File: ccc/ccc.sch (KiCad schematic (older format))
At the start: 36 parts, among them J1 Conn_02x03_Odd_Even, U1 rt9013-33, U2 LTC3225-1

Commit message: usb bridge readability update
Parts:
- added R? (x2): 10k, symbol Device:R
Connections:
- net GPIO0: now also Q?.2 (C); no longer Q?.2 (C)
- net RST: now also Q?.2 (C); no longer Q?.2 (C)
- new net: Q?.3 (E), R?.2, U?.24 (~RTS)
- new net: Q?.3 (E), R?.2, U?.28 (~DTR)
- new net: Q?.1 (B), R?.1 (x2)
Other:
- moved on the sheet: Q?, R?
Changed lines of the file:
@@
 L Device:Q_NPN_BCE Q?
 U 1 1 5D00C58E
-P 4600 4700
-F 0 "Q?" H 4791 4654 50  0000 L CNN
-F 1 "Q_NPN_BCE" H 4791 4745 50  0000 L CNN
-F 2 "" H 4800 4800 50  0001 C CNN
-F 3 "~" H 4600 4700 50  0001 C CNN
-	1    4600 4700
-	0    1    -1   0
+P 4600 5050
+F 0 "Q?" H 4791 5004 50  0000 L CNN
+F 1 "Q_NPN_BCE" H 4791 5095 50  0000 L CNN
+F 2 "" H 4800 5150 50  0001 C CNN
+F 3 "~" H 4600 5050 50  0001 C CNN
+	1    4600 5050
+	1    0    0    1
 $EndComp
 $Comp
 L Device:Q_NPN_BCE Q?
 U 1 1 5D00EDC1
-P 4600 5200
-F 0 "Q?" H 4791 5246 50  0000 L CNN
-F 1 "Q_NPN_BCE" H 4791 5155 50  0000 L CNN
-F 2 "" H 4800 5300 50  0001 C CNN
-F 3 "~" H 4600 5200 50  0001 C CNN
-	1    4600 5200
-	0    -1   1    0
-$EndComp
-Wire Wire Line
-	3350 5050 2900 5050
-Wire Wire Line
-	4400 4600 4400 5000
-Wire Wire Line
-	4400 5000 4600 5000
-Connection ~ 4400 4600
+P 4600 4400
+F 0 "Q?" H 4791 4446 50  0000 L CNN
+F 1 "Q_NPN_BCE" H 4791 4355 50  0000 L CNN
+F 2 "" H 4800 4500 50  0001 C CNN
+F 3 "~" H 4600 4400 50  0001 C CNN
+	1    4600 4400
+	1    0    0    -1
+$EndComp
 Wire Wire Line
 	2900 5450 3500 5450
-Text GLabel 5100 4600 2    50   Input ~ 0
+Text GLabel 5150 4050 2    50   Input ~ 0
 RST
-Wire Wire Line
-	4800 4600 5100 4600
-Wire Wire Line
-	4600 4900 4800 4900
-Wire Wire Line
-	4800 4900 4800 5300
-Connection ~ 4600 4900
-Text GLabel 4050 5800 3    50   Input ~ 0
+Text GLabel 5800 5250 2    50   Input ~ 0
 GPIO0
 Wire Wire Line
@@
 L Device:R R?
 U 1 1 5D0A7656
-P 4050 5400
-F 0 "R?" H 4120 5446 50  0000 L CNN
-F 1 "10k" H 4120 5355 50  0000 L CNN
-F 2 "" V 3980 5400 50  0001 C CNN
-F 3 "~" H 4050 5400 50  0001 C CNN
-	1    4050 5400
+P 5550 4800
+F 0 "R?" H 5620 4846 50  0000 L CNN
+F 1 "10k" H 5620 4755 50  0000 L CNN
+F 2 "" V 5480 4800 50  0001 C CNN
+F 3 "~" H 5550 4800 50  0001 C CNN
+	1    5550 4800
 	1    0    0    -1
 $EndComp
@@
 L power:+3V3 #PWR?
 U 1 1 5D0A810F
-P 4050 5250
-F 0 "#PWR?" H 4050 5100 50  0001 C CNN
-F 1 "+3V3" H 4065 5423 50  0000 C CNN
-F 2 "" H 4050 5250 50  0001 C CNN
-F 3 "" H 4050 5250 50  0001 C CNN
-	1    4050 5250
-	1    0    0    -1
-$EndComp
-Wire Wire Line
-	4350 5550 4350 5300
-Wire Wire Line
-	4350 5300 4400 5300
-Wire Wire Line
-	4050 5550 4350 5550
-Wire Wire Line
-	4050 5550 4050 5800
-Connection ~ 4050 5550
-Wire Wire Line
-	3350 5050 3350 4600
-Wire Wire Line
-	3350 4600 4400 4600
-Wire Wire Line
-	3500 5450 3500 4900
-Wire Wire Line
-	3500 4900 4600 4900
+P 5550 4650
+F 0 "#PWR?" H 5550 4500 50  0001 C CNN
+F 1 "+3V3" H 5565 4823 50  0000 C CNN
+F 2 "" H 5550 4650 50  0001 C CNN
+F 3 "" H 5550 4650 50  0001 C CNN
+	1    5550 4650
+	1    0    0    -1
+$EndComp
 Text GLabel 10850 3500 2    50   Input ~ 0
 GPIO0
@@
 Wire Wire Line
 	10700 3550 10600 3550
-Text GLabel 6350 5850 2    50   Input ~ 0
+Text GLabel 6300 4050 2    50   Input ~ 0
 GPIO2
 $Comp
 L Device:R R?
 U 1 1 5D15E953
-P 6200 5550
-F 0 "R?" H 6270 5596 50  0000 L CNN
-F 1 "10k" H 6270 5505 50  0000 L CNN
-F 2 "" V 6130 5550 50  0001 C CNN
-F 3 "~" H 6200 5550 50  0001 C CNN
-	1    6200 5550
+P 6150 3750
+F 0 "R?" H 6220 3796 50  0000 L CNN
+F 1 "10k" H 6220 3705 50  0000 L CNN
+F 2 "" V 6080 3750 50  0001 C CNN
+F 3 "~" H 6150 3750 50  0001 C CNN
+	1    6150 3750
 	1    0    0    -1
 $EndComp
@@
 L power:+3V3 #PWR?
 U 1 1 5D15EFF7
-P 6200 5150
-F 0 "#PWR?" H 6200 5000 50  0001 C CNN
-F 1 "+3V3" H 6215 5323 50  0000 C CNN
-F 2 "" H 6200 5150 50  0001 C CNN
-F 3 "" H 6200 5150 50  0001 C CNN
-	1    6200 5150
-	1    0    0    -1
-$EndComp
-Wire Wire Line
-	6200 5150 6200 5400
-Wire Wire Line
-	6200 5850 6350 5850
-Wire Wire Line
-	6200 5700 6200 5850
+P 6150 3350
+F 0 "#PWR?" H 6150 3200 50  0001 C CNN
+F 1 "+3V3" H 6165 3523 50  0000 C CNN
+F 2 "" H 6150 3350 50  0001 C CNN
+F 3 "" H 6150 3350 50  0001 C CNN
+	1    6150 3350
+	1    0    0    -1
+$EndComp
+Wire Wire Line
+	6150 3350 6150 3600
+Wire Wire Line
+	6150 4050 6300 4050
+Wire Wire Line
+	6150 3900 6150 4050
 Text GLabel 8900 4950 2    50   Input ~ 0
 GPIO2
@@
 Wire Wire Line
 	10700 3950 10850 3950
+$Comp
+L Device:R R?
+U 1 1 5CECFF12
+P 4050 5050
+F 0 "R?" V 3843 5050 50  0000 C CNN
+F 1 "10k" V 3934 5050 50  0000 C CNN
+F 2 "" V 3980 5050 50  0001 C CNN
+F 3 "~" H 4050 5050 50  0001 C CNN
+	1    4050 5050
+	0    1    1    0
+$EndComp
+$Comp
+L Device:R R?
+U 1 1 5CED075B
+P 4050 4400
+F 0 "R?" V 3843 4400 50  0000 C CNN
+F 1 "10k" V 3934 4400 50  0000 C CNN
+F 2 "" V 3980 4400 50  0001 C CNN
+F 3 "~" H 4050 4400 50  0001 C CNN
+	1    4050 4400
+	0    1    1    0
+$EndComp
+Wire Wire Line
+	4200 4400 4400 4400
+Wire Wire Line
+	4200 5050 4400 5050
+Wire Wire Line
+	2900 5050 3750 5050
+Wire Wire Line
+	3500 4400 3850 4400
+Wire Wire Line
+	3500 4400 3500 5450
+Wire Wire Line
+	5150 4050 4700 4050
+Wire Wire Line
+	4700 4050 4700 4200
+Wire Wire Line
+	3750 5050 3750 4600
+Wire Wire Line
+	3750 4600 4700 4600
+Connection ~ 3750 5050
+Wire Wire Line
+	3750 5050 3900 5050
+Wire Wire Line
+	4700 4850 4700 4700
+Wire Wire Line
+	4700 4700 3850 4700
+Wire Wire Line
+	3850 4700 3850 4400
+Connection ~ 3850 4400
+Wire Wire Line
+	3850 4400 3900 4400
+Wire Wire Line
+	4700 5250 5550 5250
+Wire Wire Line
+	5800 5250 5550 5250
+Connection ~ 5550 5250
+Wire Wire Line
+	5550 4950 5550 5250
 $EndSCHEMATC

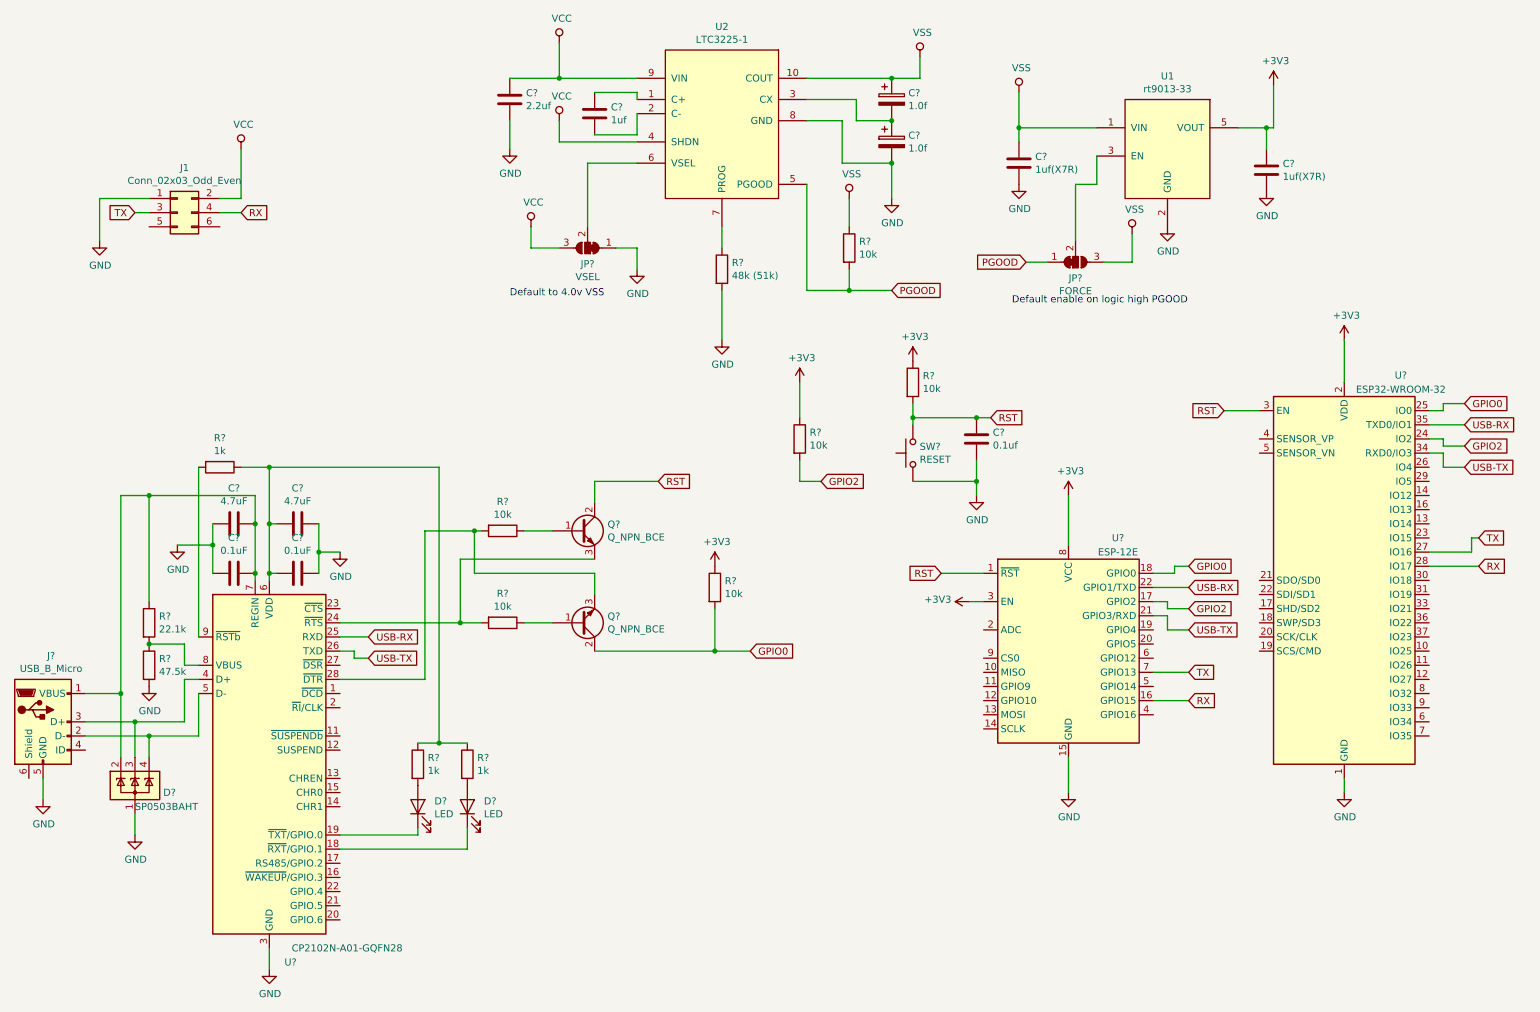
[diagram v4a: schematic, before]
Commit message: Removed usb bridge - added programming header
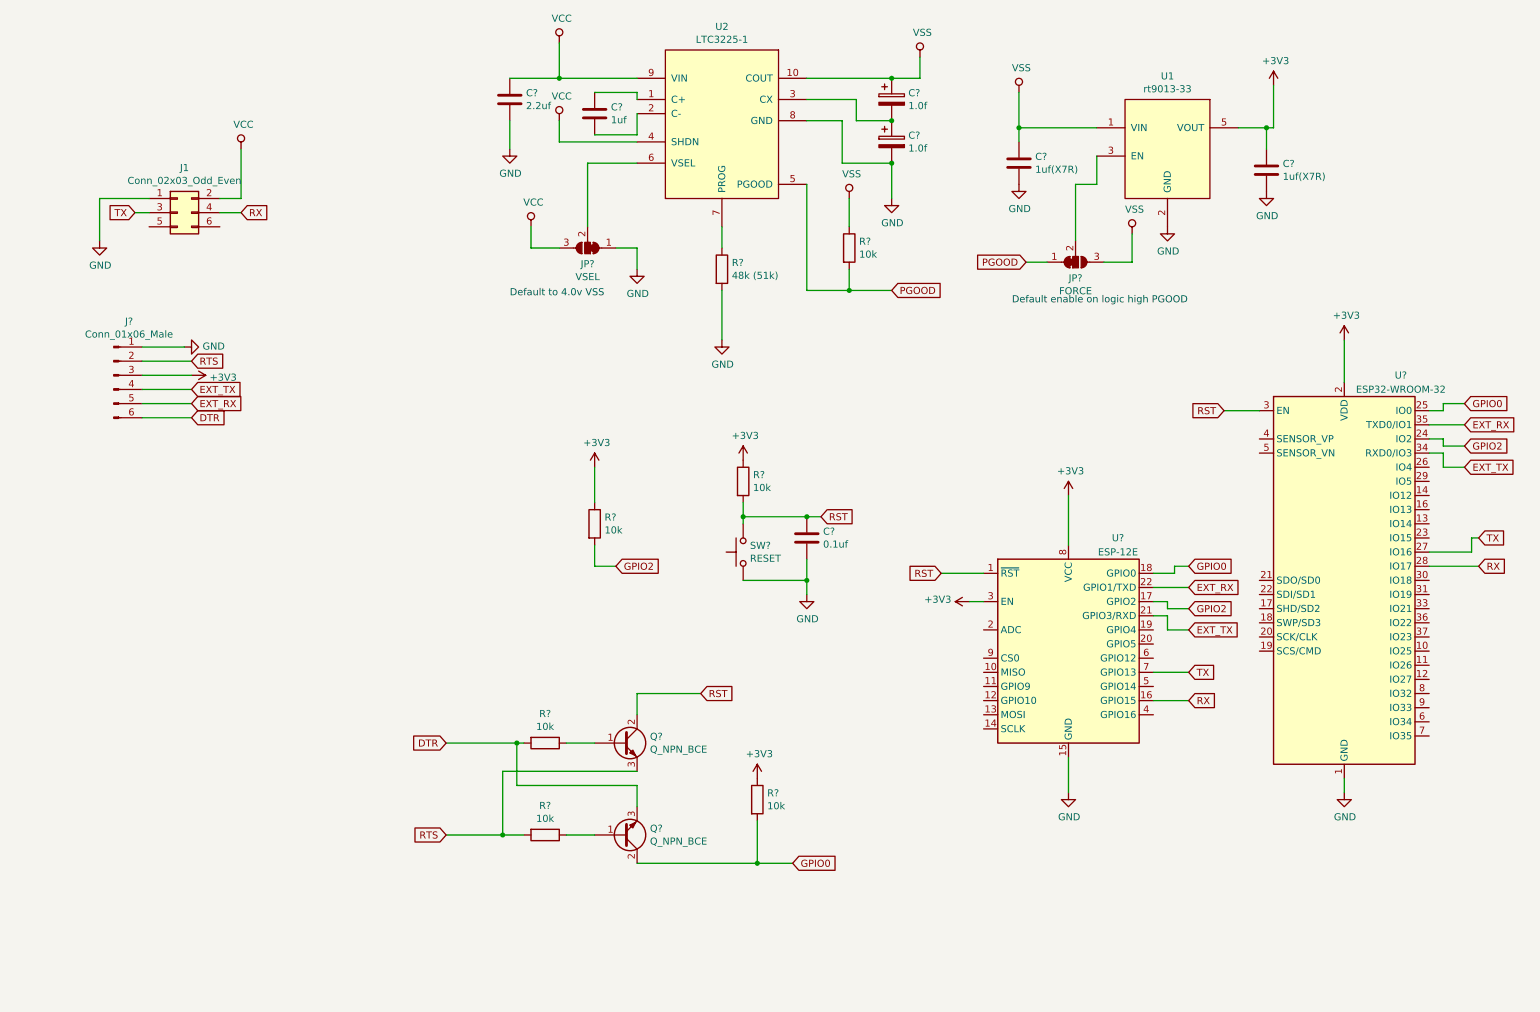
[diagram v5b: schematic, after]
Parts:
- removed C? (x2): 0.1uF, symbol Device:C
- removed C? (x2): 4.7uF, symbol Device:C
- removed D?: SP0503BAHT, Package_TO_SOT_SMD:SOT-143, symbol Power_Protection:SP0503BAHT
- removed D? (x2): LED, symbol Device:LED
- removed J?: USB_B_Micro, symbol Connector:USB_B_Micro
- removed R?: 22.1k, symbol Device:R
- removed R?: 47.5k, symbol Device:R
- removed R? (x3): 1k, symbol Device:R
- removed U?: CP2102N-A01-GQFN28, Package_DFN_QFN:QFN-28-1EP_5x5mm_P0.5mm_EP3.35x3.35mm, symbol Interface_USB:CP2102N-A01-GQFN28
- added J?: Conn_01x06_Male, symbol Connector:Conn_01x06_Male
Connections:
- net +3V3: now also J?.3 (Pin_3)
- net GND: now also J?.1 (Pin_1)
- net RTS: now reaches Q?.3 (E), R?.2
- net RTS: now also J?.2 (Pin_2)
- net DTR: now reaches Q?.3 (E), R?.2
- net DTR: now also J?.6 (Pin_6)
- net USB-RX renamed EXT_RX
- net EXT_RX: now also J?.5 (Pin_5)
- net USB-TX renamed EXT_TX
- net EXT_TX: now also J?.4 (Pin_4)
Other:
- moved on the sheet: C?, Q?, R?, SW?

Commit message: Added various testpoints and moved some autoprogramming logic resistors
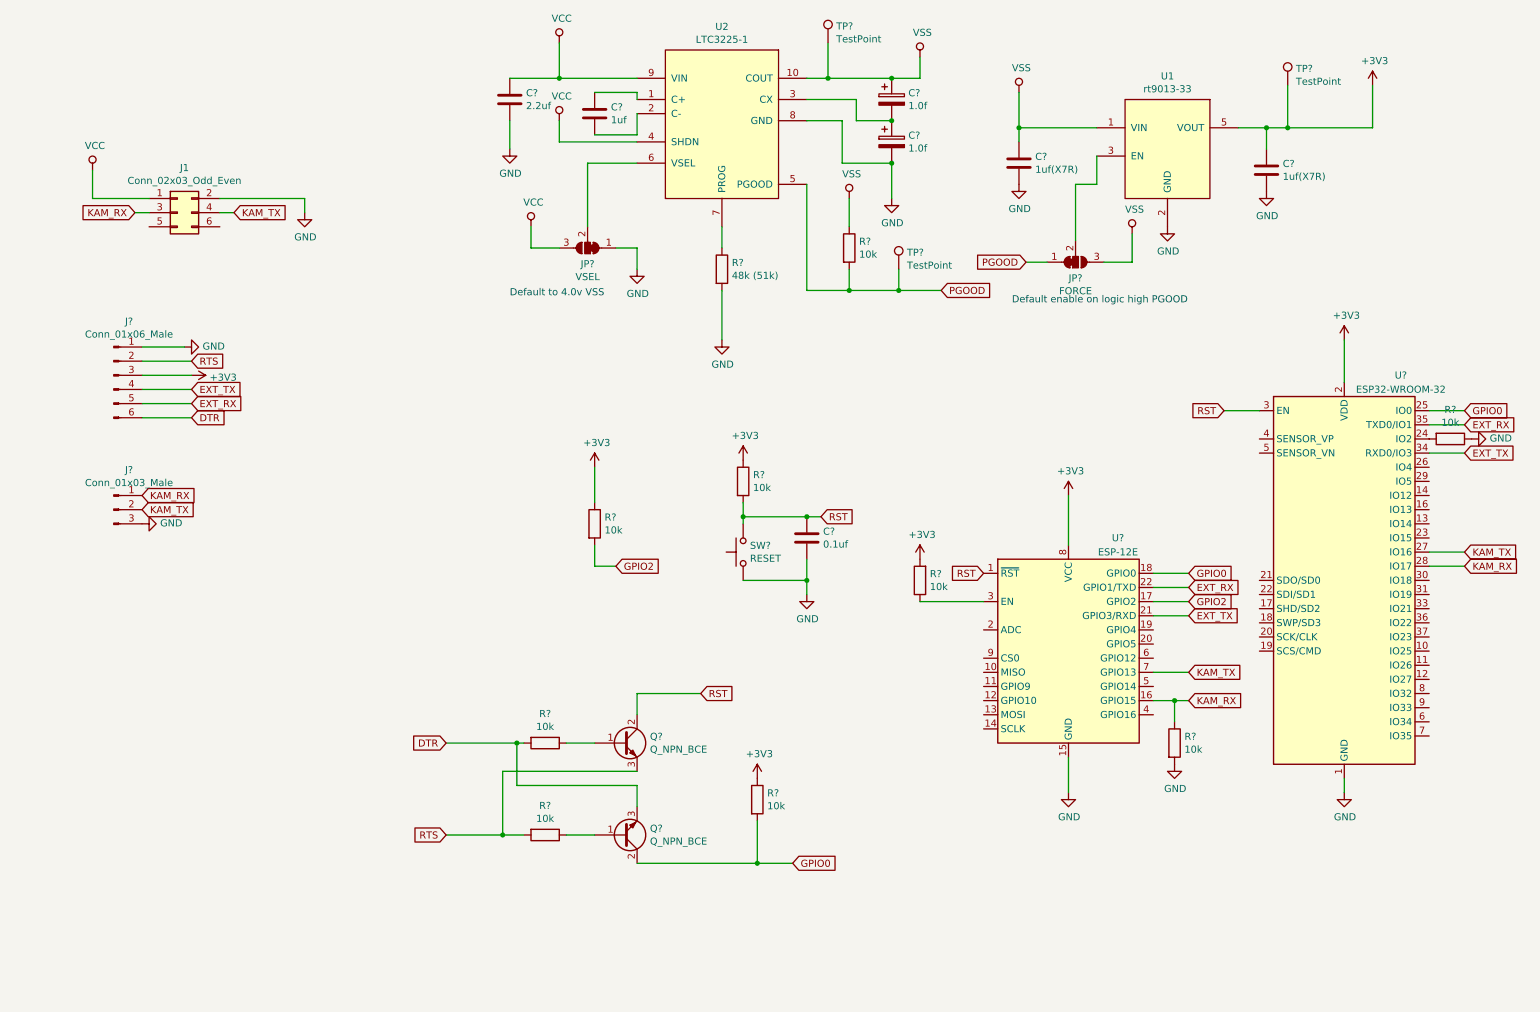
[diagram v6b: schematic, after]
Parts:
- added J?: Conn_01x03_Male, symbol Connector:Conn_01x03_Male
- added R? (x3): 10k, symbol Device:R
- added TP? (x3): TestPoint, symbol Connector:TestPoint
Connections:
- net +3V3: now also R?.2, TP?.1; no longer U?.3 (EN)
- net GND: now also J1.2 (Pin_2), J?.3 (Pin_3), R?.1, R?.2; no longer J1.1 (Pin_1)
- net GPIO2: no longer U?.24 (IO2)
- net PGOOD: now also TP?.1
- net VCC: now also J1.1 (Pin_1); no longer J1.2 (Pin_2)
- net VSS: now also TP?.1
- net RX renamed KAM_RX
- net KAM_RX: now also J1.3 (Pin_3), J?.1 (Pin_1), R?.1; no longer J1.4 (Pin_4)
- net TX renamed KAM_TX
- net KAM_TX: now also J1.4 (Pin_4), J?.2 (Pin_2); no longer J1.3 (Pin_3)
- new net: R?.1, U?.3 (EN)
- new net: R?.2, U?.24 (IO2)

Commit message: Assigned footprints for stuff
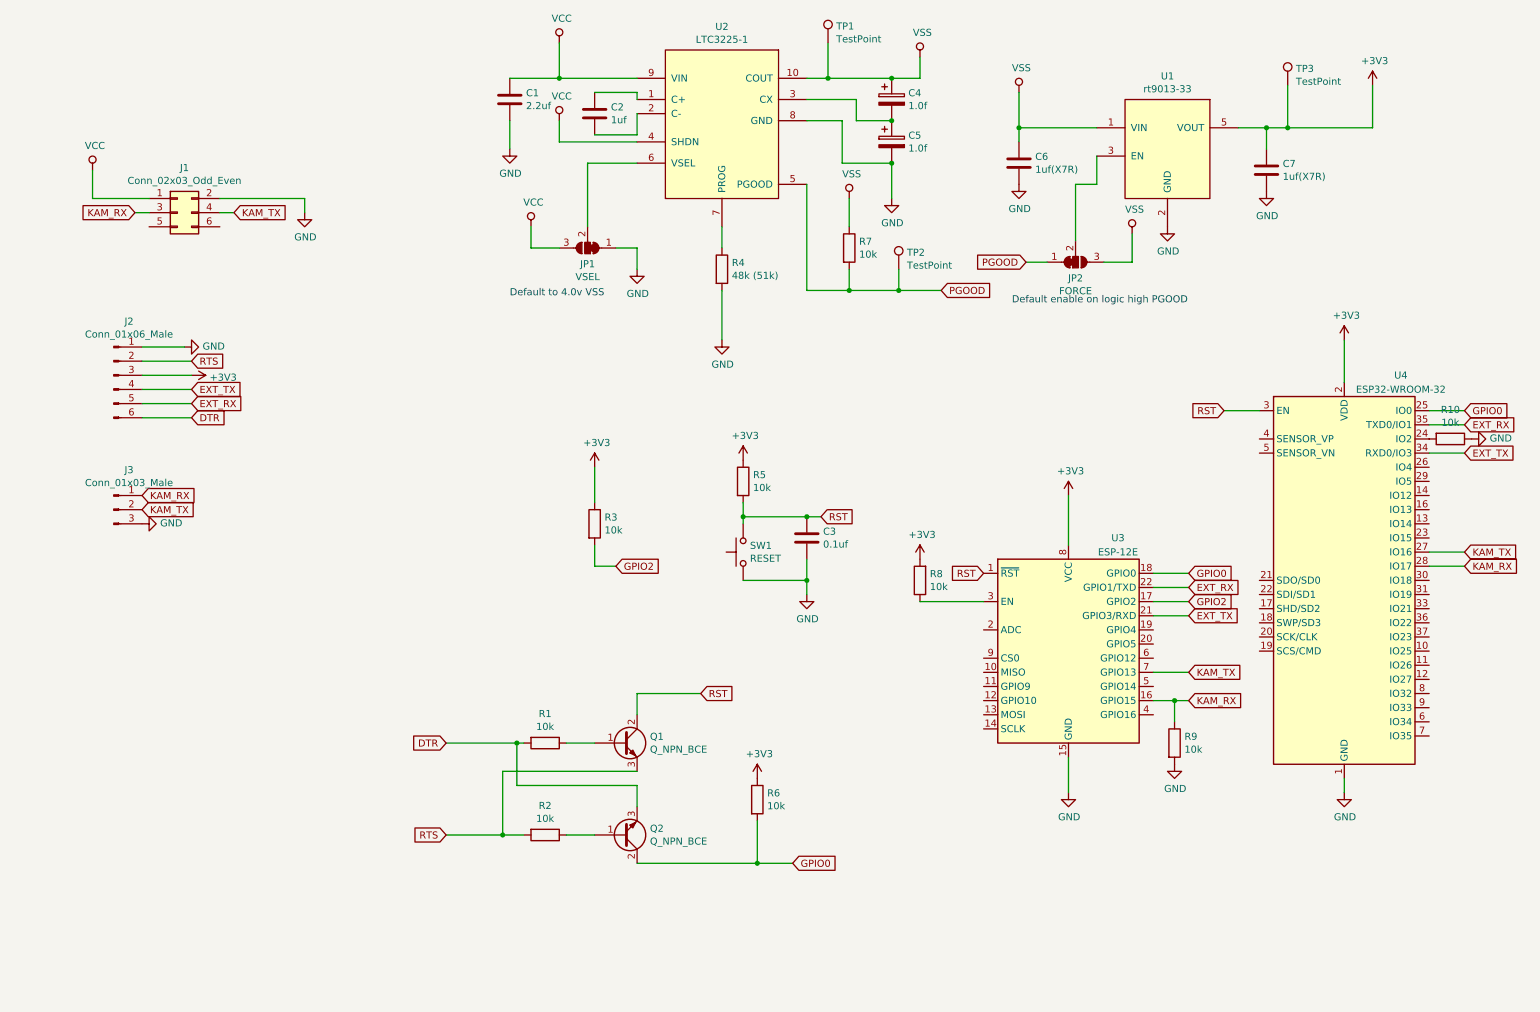
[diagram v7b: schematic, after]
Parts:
- C1, C2, C3, C6, C7: renamed from C?; footprint (none) -> Capacitor_SMD:C_1206_3216Metric_Pad1.42x1.75mm_HandSolder
- C4, C5: renamed from C?; footprint (none) -> Capacitor_THT:C_Radial_D10.0mm_H12.5mm_P5.00mm
- J2: renamed from J?; footprint (none) -> Connector_PinHeader_2.54mm:PinHeader_1x06_P2.54mm_Horizontal
- J3: renamed from J?; footprint (none) -> Connector_PinHeader_2.54mm:PinHeader_1x03_P2.54mm_Horizontal
- JP1, JP2: renamed from JP?; footprint (none) -> Jumper:SolderJumper-3_P1.3mm_Bridged12_RoundedPad1.0x1.5mm
- Q1, Q2: renamed from Q?; footprint (none) -> Package_TO_SOT_SMD:SOT-23
- R1, R10, R2, R3, R4, R5, R6, R7, R8, R9: renamed from R?; footprint (none) -> Resistor_SMD:R_0805_2012Metric
- SW1: renamed from SW?; footprint (none) -> Button_Switch_THT:SW_Tactile_SPST_Angled_PTS645Vx39-2LFS
- TP1, TP2, TP3: renamed from TP?; footprint (none) -> TestPoint:TestPoint_Pad_D2.5mm
- gave numbers to parts that had none: 2
